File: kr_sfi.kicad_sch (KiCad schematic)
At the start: 85 parts, among them U44 NTS0102_TSSOP, U45 TLK10232CTR, Y3 Oscillator_156.25MHz_SG3225EEN

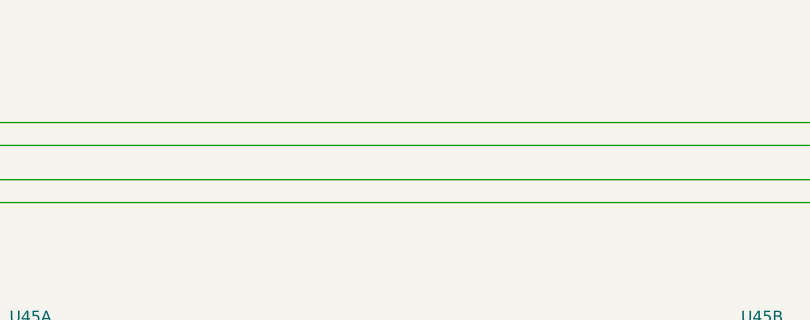
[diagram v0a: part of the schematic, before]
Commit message: [#70030] Unify functional block names
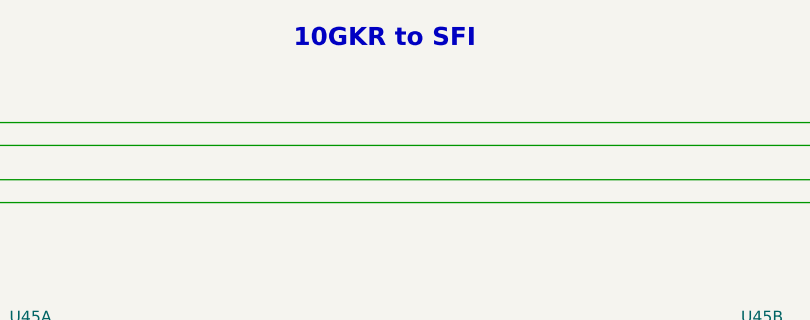
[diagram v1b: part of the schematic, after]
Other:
- note added: "10GKR to SFI"
- company: Antmicro Ltd. -> Antmicro Ltd
- title: Com Express 7 baseboard -> COM Express 7 Baseboard
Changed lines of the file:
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@@
 	(paper "A3")
 	(title_block
-		(title "Com Express 7 baseboard")
-		(date "2024-03-28")
+		(title "COM Express 7 Baseboard")
+		(date "2024-12-13")
 		(rev "1.1.0")
-		(company "Antmicro Ltd.")
+		(company "Antmicro Ltd")
+		(comment 1 "www.antmicro.com")
 	)
 	(bus_alias "SFI"
@@
 			)
 			(justify left bottom)
+		)
+	)
+	(text "10GKR to SFI"
+		(exclude_from_sim no)
+		(at 195.58 33.782 0)
+		(effects
+			(font
+				(size 2 2)
+				(thickness 0.4)
+				(bold yes)
+			)
+			(justify left bottom)
